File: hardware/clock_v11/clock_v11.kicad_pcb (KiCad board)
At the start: 2 copper layers, 119 x 92 mm, 227 parts, among them J1 RJ45, J10 KH-BNC50-3511, J11 KH-BNC50-3511, J12 Conn_01x03_Pin, J13 KH-BNC50-3511, J14 DC-005B-2.5A-2.0, J2 Conn_01x03, J3 KH-BNC50-3511, J4 USB_C_Receptacle, J5 Conn_01x06_Pin, J6 Conn_01x03_Pin, J7 KH-BNC50-3511, J8 Conn_01x02_Pin, J9 KH-BNC50-3511, Q1 2N7002, Q10 2N7002, Q9 2N7002, SW1 SW_Push_4PDT, U1 ADA4807-1, U10 STM32F405RGTx, U11 AMS1117-3.3, U12 BA50DD0WHFP-TR, U13 M24C02-RMN, U14 CH340C, U15 USBLC6-2P6, U16 TLV3603DCKR, U17 SN74LVC1G14DBV, U18 TMP112AIDRLR, U19 SN74LVC1G14DBV, U2 SN74LVC1G14DBV, U20 SN74LVC1G14DBV, U21 SN74LVC1G14DBV, U23 TPS63060, U3 SN74LVC1G14DBV, U4 ADA4807-1, U5 ADA4807-1, U6 TLV3603DCKR, U7 SN74LVC1G14DBV, U8 TLV3603DCKR, U9 L78L05_SOT89, Y1 AOCJY4A-10.000MHZ-SW, Y2 16MHz

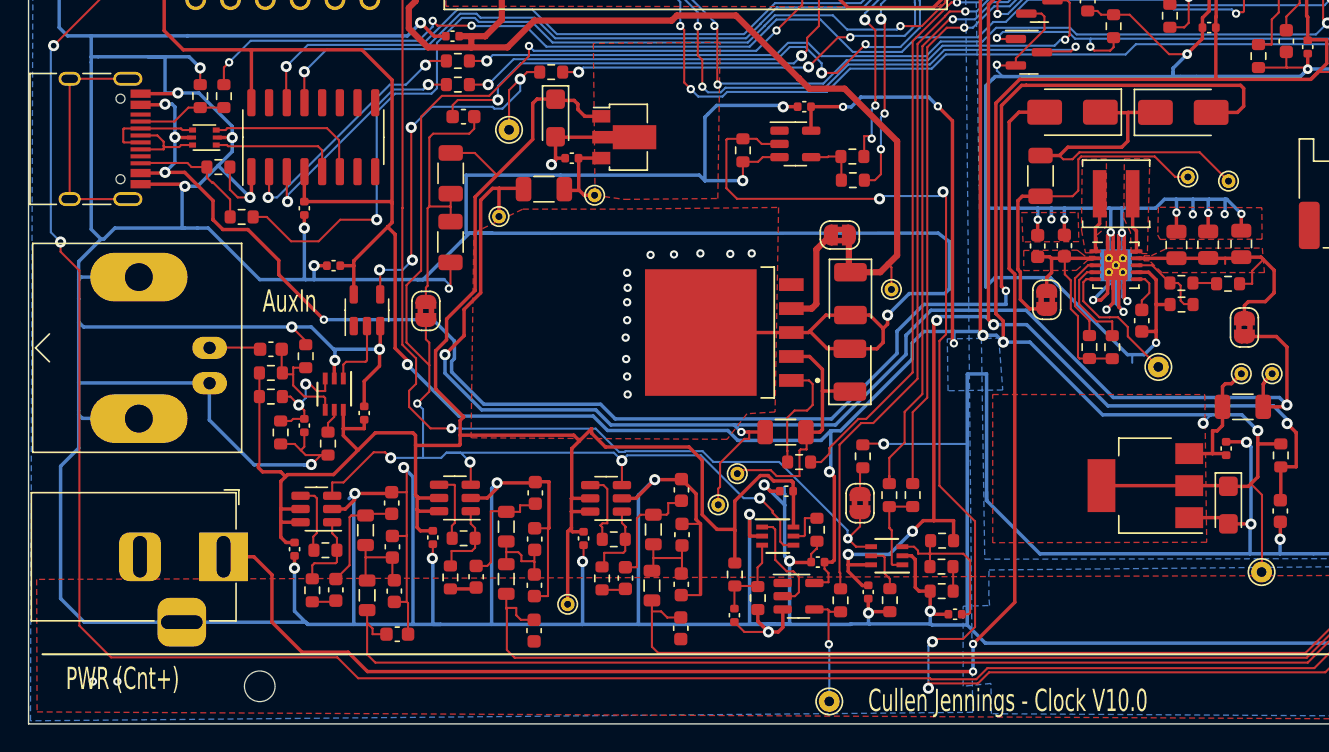
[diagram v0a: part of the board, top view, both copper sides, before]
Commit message: make clock board USB power only. Fixes #307
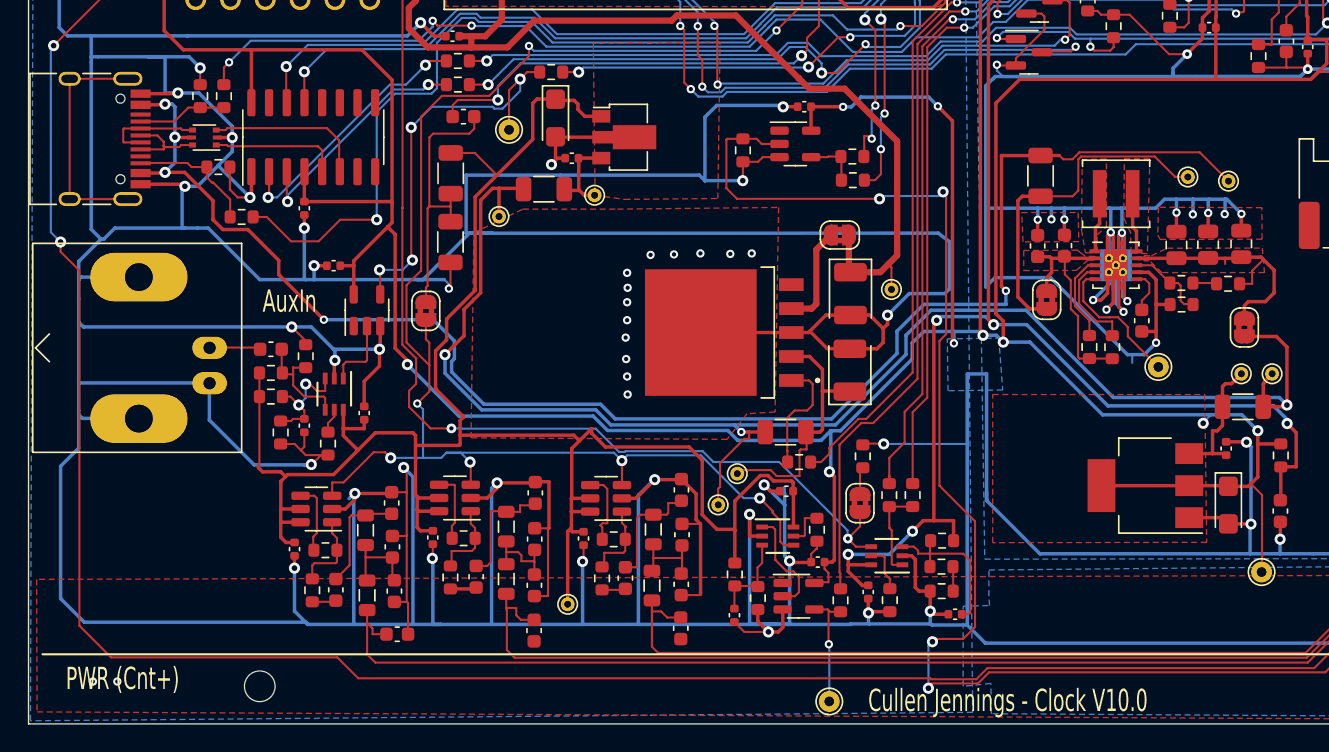
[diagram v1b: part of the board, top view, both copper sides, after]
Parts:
- removed D1, D2: SS34, Diode_SMD:D_SMA
- removed J14: DC-005B-2.5A-2.0, Connector_BarrelJack:BarrelJack_Horizontal
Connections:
- R42 pad 2: Net-(D1-K) -> VBUS
- TP9 pad 1: Net-(D1-K) -> VBUS
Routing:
- net +BATT: track 102.9 -> 0.00 mm, vias 2 -> 0
- net Net-(D1-K): track 26.0 -> 0.00 mm
- net VBUS: track 121.9 -> 113.9 mm

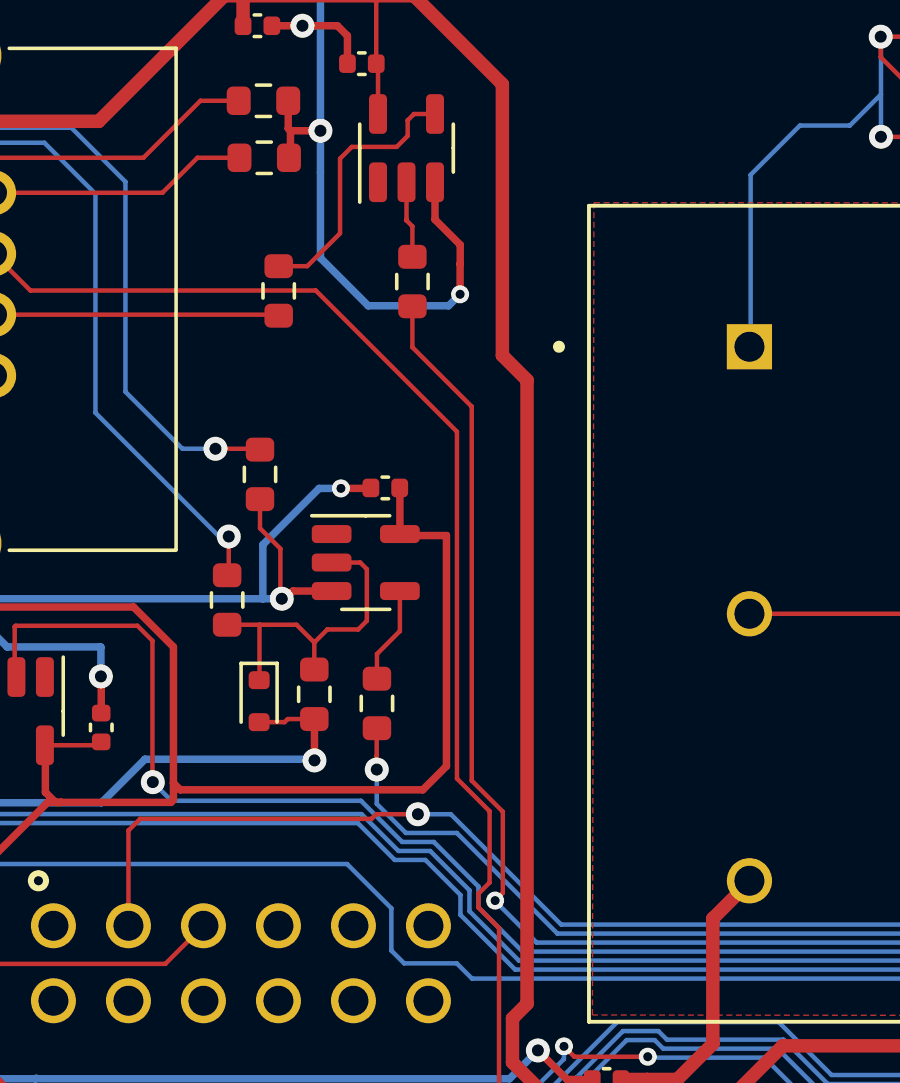
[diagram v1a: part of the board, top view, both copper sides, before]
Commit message: Remove R49. Fixes #303
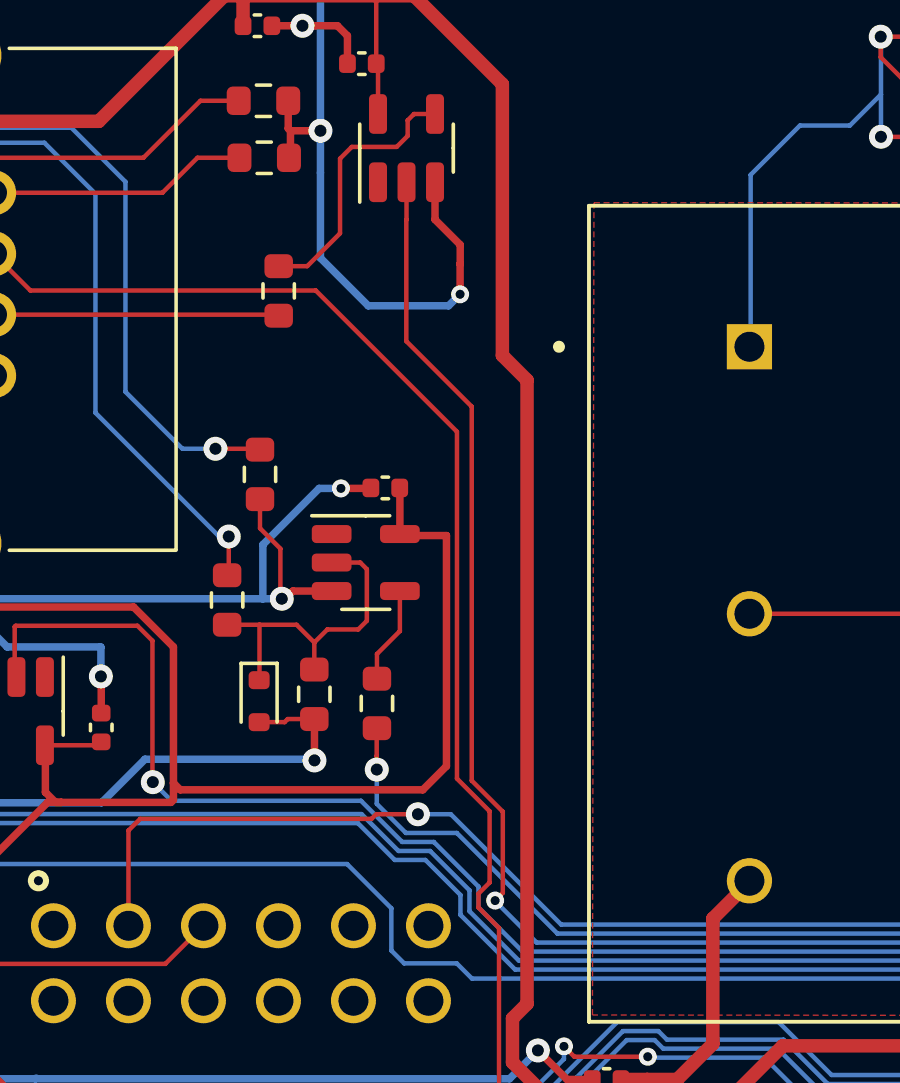
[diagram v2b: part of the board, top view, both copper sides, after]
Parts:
- removed R49: 1K0, Resistor_SMD:R_0603_1608Metric
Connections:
- U19 pad 2: Net-(R49-Pad2) -> /GPS_RX1
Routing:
- net /GPS_RX1: track 94.7 -> 99.0 mm
- net Net-(R49-Pad2): track 2.58 -> 0.00 mm

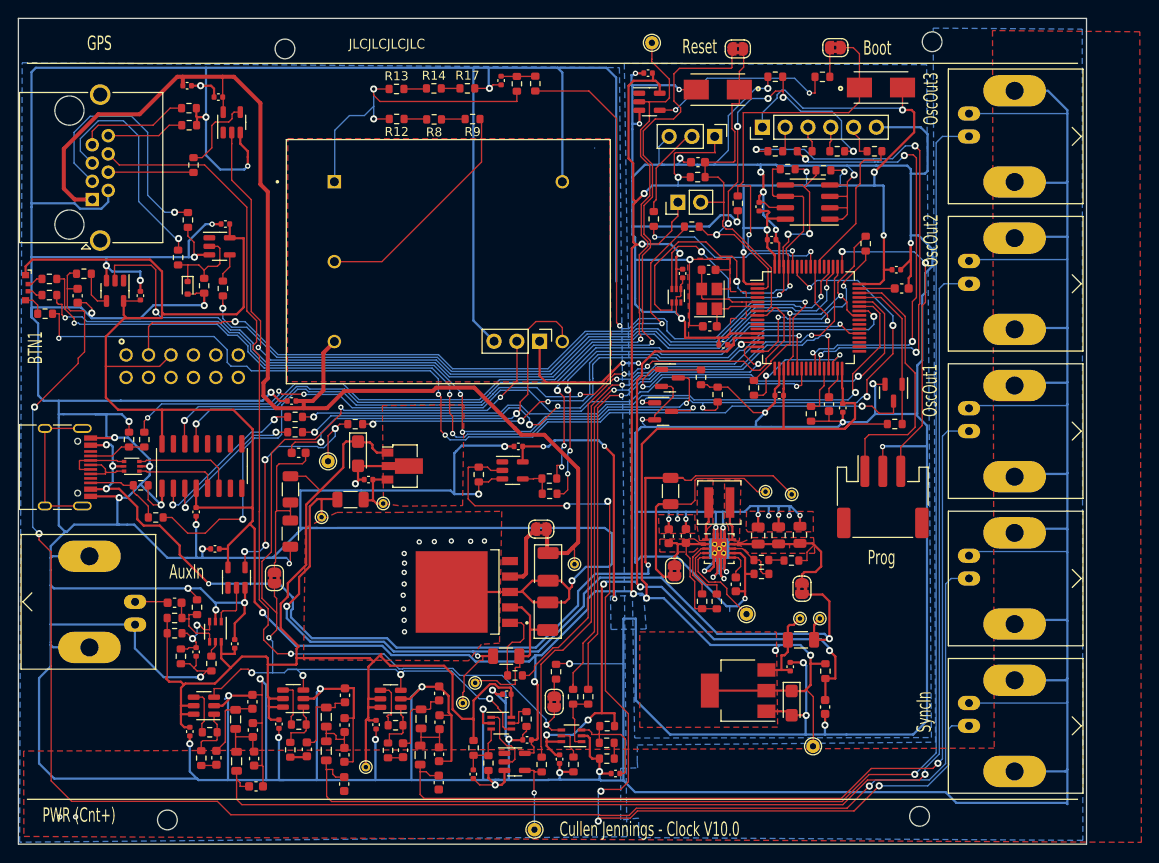
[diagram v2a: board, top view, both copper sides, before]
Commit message: remove needless pull down reistors. Fixes #304
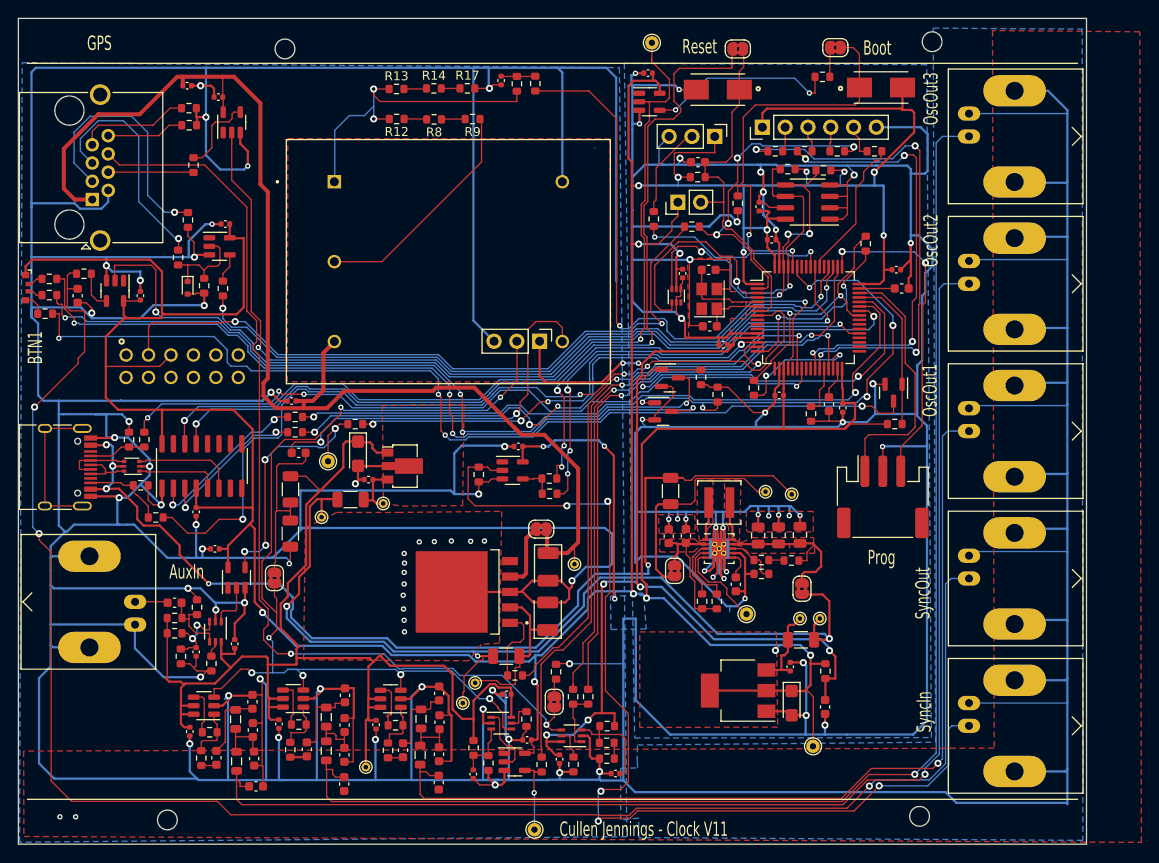
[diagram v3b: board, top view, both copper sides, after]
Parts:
- removed R40: 4K7, Resistor_SMD:R_0603_1608Metric
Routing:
- net GND: track 1615.9 -> 1603.1 mm, vias 92 -> 91
- net /BTN1: track 48.3 -> 37.5 mm, vias 6 -> 4
- net +3.3V: track 515.6 -> 513.2 mm, vias 20 -> 19
- net /USB_RTS: track 97.7 -> 96.4 mm
- net /NRST: track 41.8 -> 40.5 mm
- net /USB_DTR: track 108.7 -> 107.4 mm
- net /DB3: track 16.8 -> 16.0 mm
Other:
- board text added: "Cullen Jennings - Clock V11"
- board text added: "SyncOut"
- board text removed: "Cullen Jennings - Clock V10.0"
- board text removed: "JLCJLCJLCJLC"
- board text removed: "PWR (Cnt+)"

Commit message: update with sockets for differnt oscilators
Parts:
- removed J12: Conn_01x03_Pin, Connector_PinHeader_2.54mm:PinHeader_1x03_P2.54mm_Vertical
- Y1: value AOCJY4A-10.000MHZ-SW -> MultiOsc; footprint blinky_footprints:XTAL_AOCJY4A-10.000MHZ-SW -> blinky_footprints:XTAL_Multi
- moved Y1 0.40 mm to (142.9, 64.7)
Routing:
- net +3.3VA: track 121.6 -> 154.4 mm
- net /Vadj: track 35.9 -> 65.3 mm
- net /10Mhz2.5V: track 110.0 -> 133.3 mm
- net GND: track 1603.1 -> 1625.8 mm, vias 91 -> 98
- net +3.3V: track 513.2 -> 512.0 mm
- net Net-(J5-Pin_5): track 3.80 -> 3.18 mm

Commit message: chance current sense resistor. Fixes#308
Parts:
- R42: value 0R1 -> 0R020
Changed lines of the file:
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@@
     (descr "Resistor SMD 1206 (3216 Metric), square (rectangular) end terminal, IPC_7351 nominal, (Body size source: IPC-SM-782 page 72, https://www.pcb-3d.com/wordpress/wp-content/uploads/ipc-sm-782a_amendment_1_and_2.pdf), generated with kicad-footprint-generator")
     (tags "resistor")
-    (property "JLCPCB Part #" "C25334")
+    (property "JLCPCB Part #" "C2765435")
     (property "Sheetfile" "clock_v11.kicad_sch")
     (property "Sheetname" "")
@@
         (effects (font (size 1 1) (thickness 0.15)))
     )
-    (fp_text value "0R1" (at 0 1.82 90) (layer "F.Fab")
+    (fp_text value "0R020" (at 0 1.82 90) (layer "F.Fab")
         (effects (font (size 1 1) (thickness 0.15)))
     )

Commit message: fix up footprints
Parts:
- U23: footprint Package_SON:Texas_S-PWSON-N10_ThermalVias -> blinky_footprints:Texas_S-PWSON-N10_ThermalVias-CJ
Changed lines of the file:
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@@
     )
   )
-  (footprint "Package_SON:Texas_S-PWSON-N10_ThermalVias" (layer "F.Cu")
+  (footprint "blinky_footprints:Texas_S-PWSON-N10_ThermalVias-CJ" (layer "F.Cu")
     (at 173.073016 97.070679)
     (descr "3x3mm Body, 0.5mm Pitch, S-PWSON-N10, DSC, http://www.ti.com/lit/ds/symlink/tps63060.pdf")
@@
     (pad "11" smd rect (at -0.001 0) (size 2.3 2.3) (layers "B.Cu")
       (net 26 "GND") (pinfunction "PGND") (pintype "power_in"))
-    (pad "11" thru_hole circle (at 0 0) (size 0.6 0.6) (drill 0.3) (layers "*.Cu" "*.Mask")
-      (net 26 "GND") (pinfunction "PGND") (pintype "power_in"))
     (pad "11" smd rect (at 0 0) (size 1.7 2.15) (layers "F.Cu" "F.Mask")
       (net 26 "GND") (pinfunction "PGND") (pintype "power_in"))
@@
     (fp_circle (center 1.5 -0.5) (end 1.6 -0.5)
       (stroke (width 0.508) (type solid)) (fill none) (layer "F.SilkS"))
-    (fp_line (start -4.75 -6.2) (end -4.75 14)
+    (fp_line (start -4.75 -6.2) (end -4.75 16)
       (stroke (width 0.1524) (type solid)) (layer "F.CrtYd"))
     (fp_line (start -4.75 -6.2) (end -2.5 -6.2)
       (stroke (width 0.15) (type default)) (layer "F.CrtYd"))
-    (fp_line (start -4.75 14) (end 2.25 14)
+    (fp_line (start -4.75 16) (end 2.25 16)
       (stroke (width 0.1524) (type solid)) (layer "F.CrtYd"))
     (fp_line (start -2.5 -16.7) (end -2.5 -6.2)
@@
     (fp_line (start 0 -6.2) (end 2.25 -6.2)
       (stroke (width 0.15) (type default)) (layer "F.CrtYd"))
-    (fp_line (start 2.25 14) (end 2.25 -6.2)
+    (fp_line (start 2.25 16) (end 2.25 -6.2)
       (stroke (width 0.1524) (type solid)) (layer "F.CrtYd"))
     (fp_line (start 2.5019 -3.4036) (end -2.5019 -3.4036)

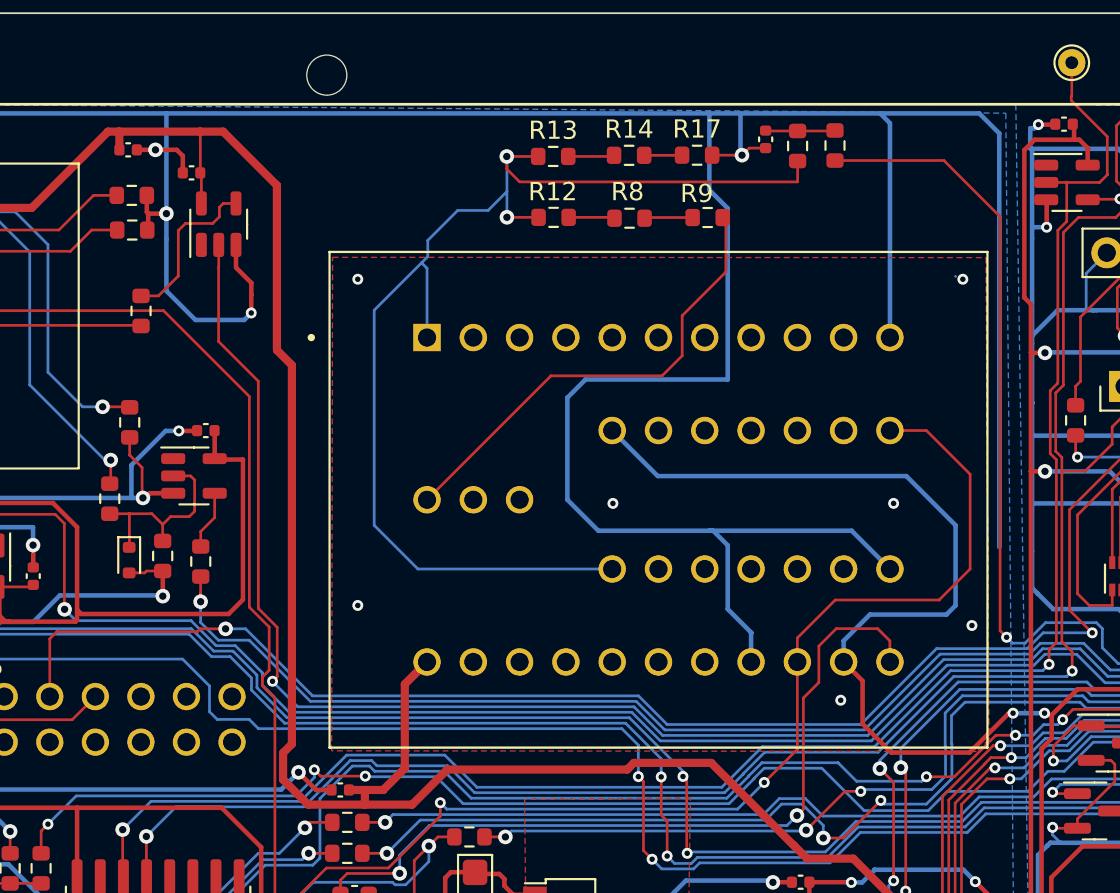
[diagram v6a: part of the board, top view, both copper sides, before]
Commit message: add GPS hdr to clock board
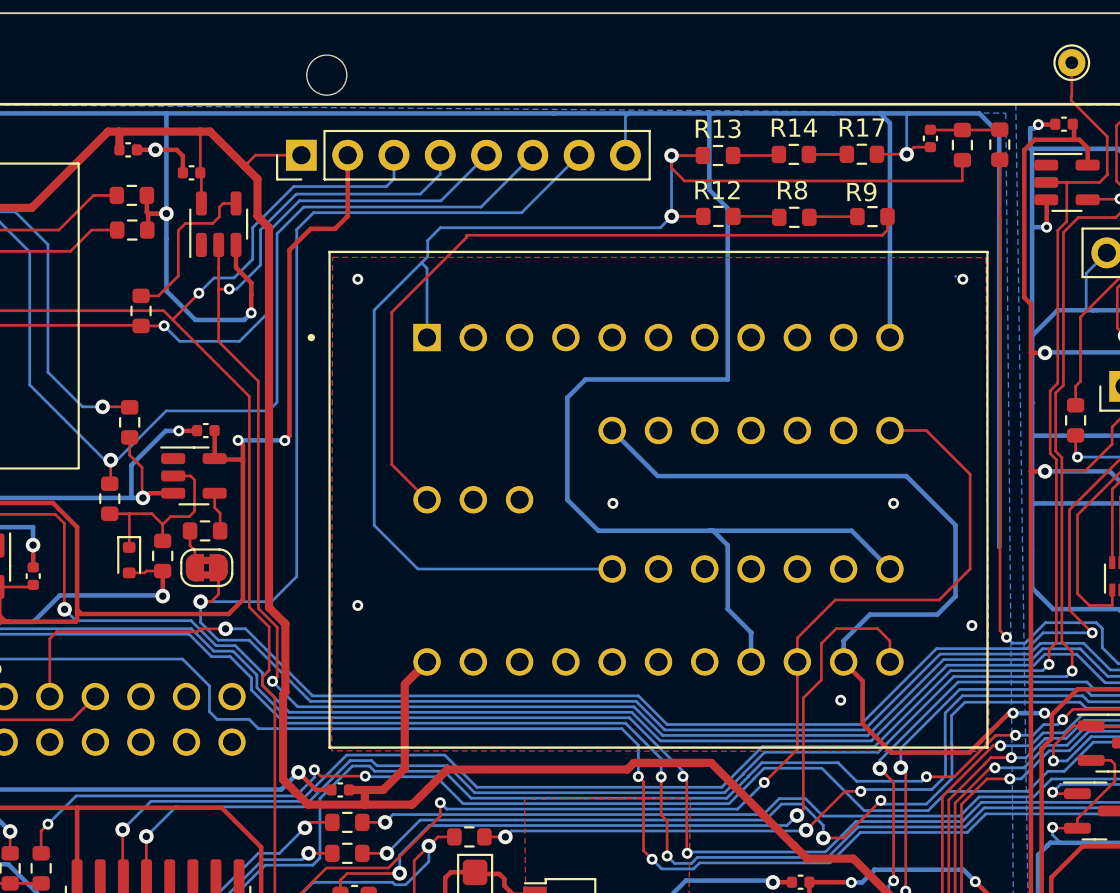
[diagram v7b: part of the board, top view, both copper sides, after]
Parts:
- added J12: Conn_01x08_Pin, Connector_PinHeader_2.54mm:PinHeader_1x08_P2.54mm_Vertical, F.Cu at (123.3, 45.8)
- added JP7: SolderJumper_2_Bridged, Jumper:SolderJumper-2_P1.3mm_Bridged2Bar_RoundedPad1.0x1.5mm, F.Cu at (118.1, 68.4)
- moved R13 9.04 mm to (146.2, 45.8)
- moved R14 9.04 mm to (150.3, 45.7)
- moved R8 9.04 mm to (150.4, 49.2)
- moved C26 9.04 mm to (157.8, 44.9)
- moved R12 9.04 mm to (146.2, 49.2)
- moved R17 9.04 mm to (154.1, 45.7)
- moved R23 9.04 mm to (159.6, 45.2)
- moved R24 9.04 mm to (161.6, 45.2)
- moved R9 9.04 mm to (154.6, 49.2)
- moved R52 1.70 mm to (118.0, 66.4), turned to 0 degrees
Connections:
- R52 pad 1: /GPS_TX1 -> Net-(JP7-A)
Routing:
- net /GPS_TX1: track 80.4 -> 123.7 mm
- net /GPS_TX1H: track 26.0 -> 61.5 mm
- net /GPS_RX1H: track 9.47 -> 35.6 mm, vias 0 -> 1
- net +3.3V: track 512.0 -> 533.8 mm, vias 19 -> 21
- net /GPS_EXT_PPS: track 107.6 -> 125.3 mm, vias 2 -> 3
- net /GPS_RX1: track 99.0 -> 115.9 mm, vias 2 -> 3
- net Net-(Y1-VREF): track 25.8 -> 41.0 mm
- net /Vadj: track 65.3 -> 73.7 mm
- net OSC_ADJ: track 66.3 -> 59.1 mm
- net +5V: track 140.1 -> 142.8 mm
- net GND: track 1625.8 -> 1628.1 mm
- net Net-(JP7-A): track 0.00 -> 2.13 mm
- net Net-(R52-Pad2): track 3.24 -> 2.19 mm
